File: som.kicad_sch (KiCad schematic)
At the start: 39 parts, among them J10 Conn_FFC_Molex_5051101097, J15 Bus_DDR4_SODIMM_CUSTOM_Jetson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, M2 Jetson-Nano, T2 BSS138PW, T4 BSS138PW, T5 BSS138PW

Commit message: [#57913] fix 2309413-1
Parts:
- BAT1: footprint jetson-nano-baseboard-footprints:MS621FE-FL11E -> antmicro-footprints:MS621FE-FL11E; symbol jetson-nano-baseboard:Battery_Holder_MS621FE-FL11E -> antmicroBatteryHoldersClipsContacts:Battery_Holder_MS621FE-FL11E
- BOOT1, PWR1, USER1: footprint jetson-nano-baseboard-footprints:LED_0603_1608Metric_G -> antmicro-footprints:LED_0603_1608Metric_G; symbol jetson-nano-baseboard:LED_G_0603_LG_L29K-G2J1-24-Z -> antmicroLEDIndicationDiscrete:LED_G_0603_LG_L29K-G2J1-24-Z
- C10, C11: footprint jetson-nano-baseboard-footprints:C_Pol_EIA-B -> antmicro-footprints:C_Pol_EIA-B; symbol jetson-nano-baseboard:C_Pol_330u_6.3V_KEMET-T520-B -> antmicroCapacitorspol:C_Pol_330u_6.3V_KEMET-T520-B
- FB2: footprint jetson-nano-baseboard-footprints:FB_1206_3216Metric -> antmicro-footprints:FB_1206_3216Metric; symbol jetson-nano-baseboard:FB_10Z_10A_WE-MPSB_1206 -> antmicroFerriteBeadsandChips:FB_10Z_10A_WE-MPSB_1206
- J10: footprint jetson-nano-baseboard-footprints:Conn_FFC_Molex_5051101097 -> antmicro-footprints:Conn_FFC_Molex_5051101097; symbol jetson-nano-baseboard:Conn_FFC_Molex_5051101097 -> antmicroFCCConnectors:Conn_FFC_Molex_5051101097
- J15: footprint jetson-nano-baseboard-footprints:TE_2309413 -> antmicro-footprints:TE_2309413; symbol jetson-nano-baseboard:Bus_DDR4_SODIMM_CUSTOM_Jetson-Nano-H9.2mm-socket -> antmicroSoMConnectors:Bus_DDR4_SODIMM_CUSTOM_Jetson-Nano-H9.2mm-socket
- M2: footprint jetson-nano-baseboard-footprints:Module_Jetson-Nano -> antmicro-footprints:Module_Jetson-Nano; symbol jetson-nano-baseboard:Jetson-Nano -> antmicroModules:Jetson-Nano
- R111, R14, R97: footprint jetson-nano-baseboard-footprints:R_0402_1005Metric -> antmicro-footprints:R_0402_1005Metric; symbol jetson-nano-baseboard:R_470R_0402 -> antmicroResistors0402:R_470R_0402
- R112, R113, R139: footprint jetson-nano-baseboard-footprints:R_0402_1005Metric -> antmicro-footprints:R_0402_1005Metric; symbol jetson-nano-baseboard:R_100k_0402 -> antmicroResistors0402:R_100k_0402
- REC1, RST1, USR1: footprint jetson-nano-baseboard-footprints:SW_TL3340AF160QG_SMD -> antmicro-footprints:SW_TL3340AF160QG_SMD; symbol jetson-nano-baseboard:SW_TL3340AF160QG_SMD -> antmicroPushbuttonSwitches:SW_TL3340AF160QG_SMD
- SP1, SP2, SP3, SP4, SP5, SP6: footprint jetson-nano-baseboard-footprints:Spacer_Drill3.7mm_H6mm_9774060151R -> antmicro-footprints:Spacer_Drill3.7mm_H6mm_9774060151R; symbol jetson-nano-baseboard:Spacer_Drill3.7mm_H6mm_9774060151R -> antmicroMechanicalParts:Spacer_Drill3.7mm_H6mm_9774060151R
- T2, T4, T5: footprint jetson-nano-baseboard-footprints:SC70-3 -> antmicro-footprints:SC70-3; symbol jetson-nano-baseboard:BSS138PW -> antmicroTransistorsFETsMOSFETsSingle:BSS138PW
- TP13, TP14, TP23, TP24, TP27, TP28, TP29, TP31, TP37, TP38, TP39: footprint jetson-nano-baseboard-footprints:TP_SMD_1.5mm -> antmicro-footprints:TP_SMD_1.5mm; symbol jetson-nano-baseboard:TP_1.5mm_SMD -> antmicroTestPoints:TP_1.5mm_SMD

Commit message: [#83358] Update KiCad project files
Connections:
- net GND: now also BAT1.2 (-); no longer BAT1.-, C10.2, C11.2, REC1.SH, RST1.SH, USR1.SH
- net PMIC_BBAT: now also BAT1.1 (+); no longer BAT1.+
- net at USER1.2 (A): no longer T5.3 (D)
- net at PWR1.2 (A): no longer T4.3 (D)
- net at BOOT1.2 (A): no longer T2.3 (D)
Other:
- moved on the sheet: C10, C11

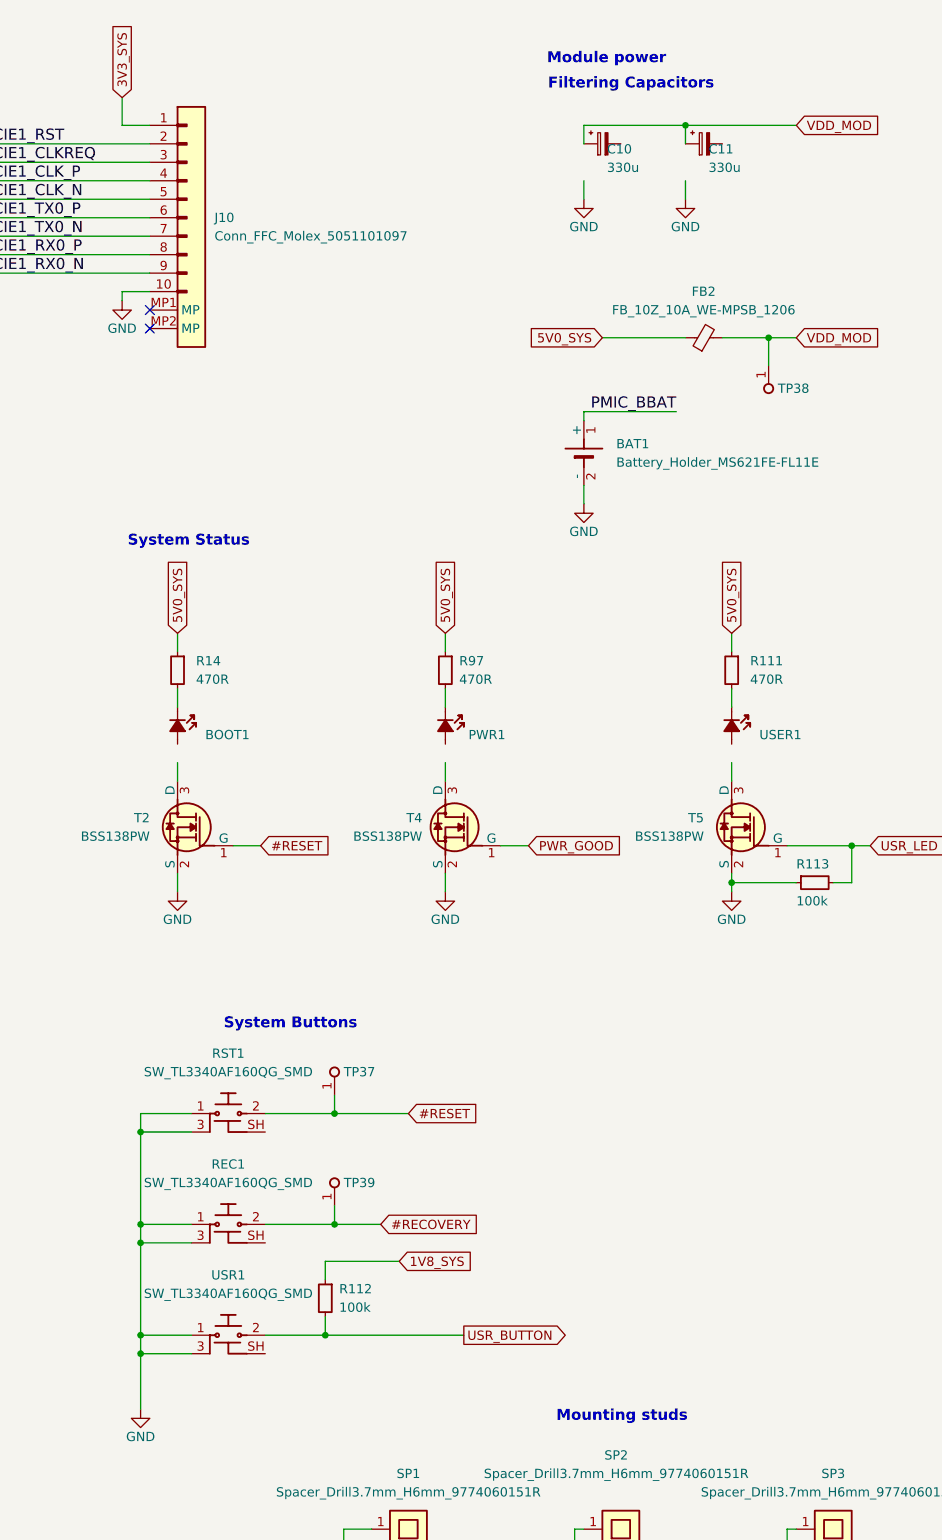
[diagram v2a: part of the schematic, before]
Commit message: [#83358] Repair broken symbol after update
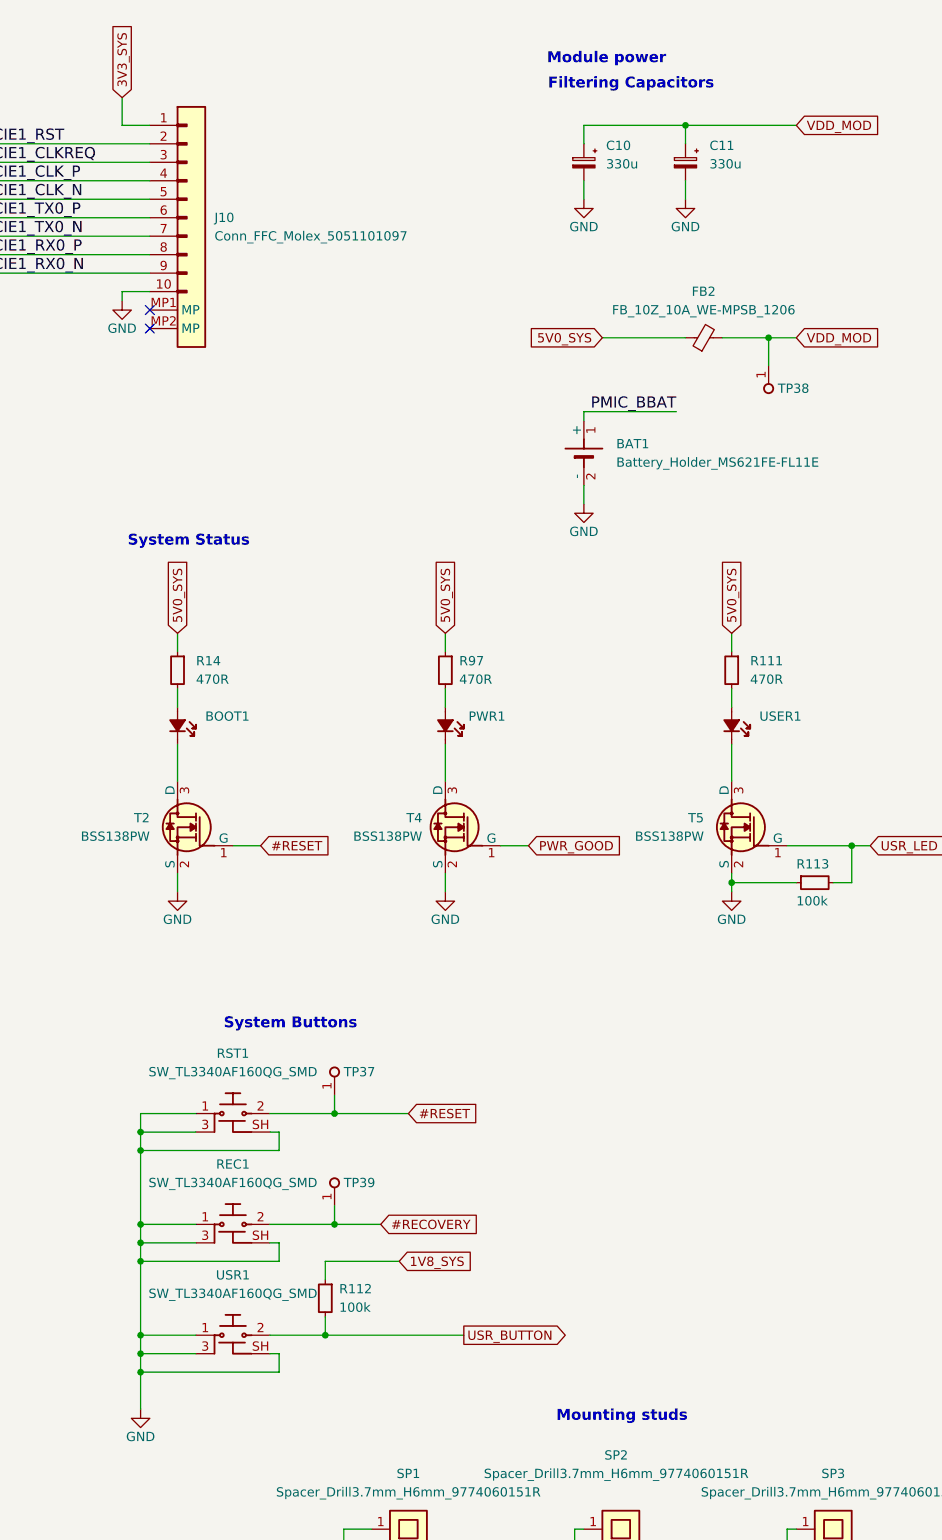
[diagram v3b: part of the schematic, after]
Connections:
- net GND: now also C10.2, C11.2, REC1.SH, RST1.SH, USR1.SH
- net at USER1.1 (C): now also T5.3 (D); no longer R111.2
- net at USER1.2 (A): now also R111.2
- net at PWR1.1 (C): now also T4.3 (D); no longer R97.2
- net at PWR1.2 (A): now also R97.2
- net at BOOT1.1 (C): now also T2.3 (D); no longer R14.2
- net at BOOT1.2 (A): now also R14.2
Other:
- moved on the sheet: C10, C11, REC1, RST1, USR1

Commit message: [#83366] Remove SoM and Tag Connect from vis
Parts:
- M2: now left out of the parts list
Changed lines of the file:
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@@
 		(unit 1)
 		(exclude_from_sim no)
-		(in_bom yes)
+		(in_bom no)
 		(on_board yes)
 		(dnp no)
